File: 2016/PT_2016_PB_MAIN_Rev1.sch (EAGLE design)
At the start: 126 parts, among them Q1 Q_IRFS7437PbF, Q11 Q_IRFS7437PbF, Q12 2N7002, Q14 Q_IRFS7437PbF, Q16 Q_IRFS7437PbF, Q2 2N7002, Q20 Q_IRFS7437PbF, Q6 Q_IRFS7437PbF, Q7 Q_IRFS7437PbF, Q9 Q_IRFS7437PbF

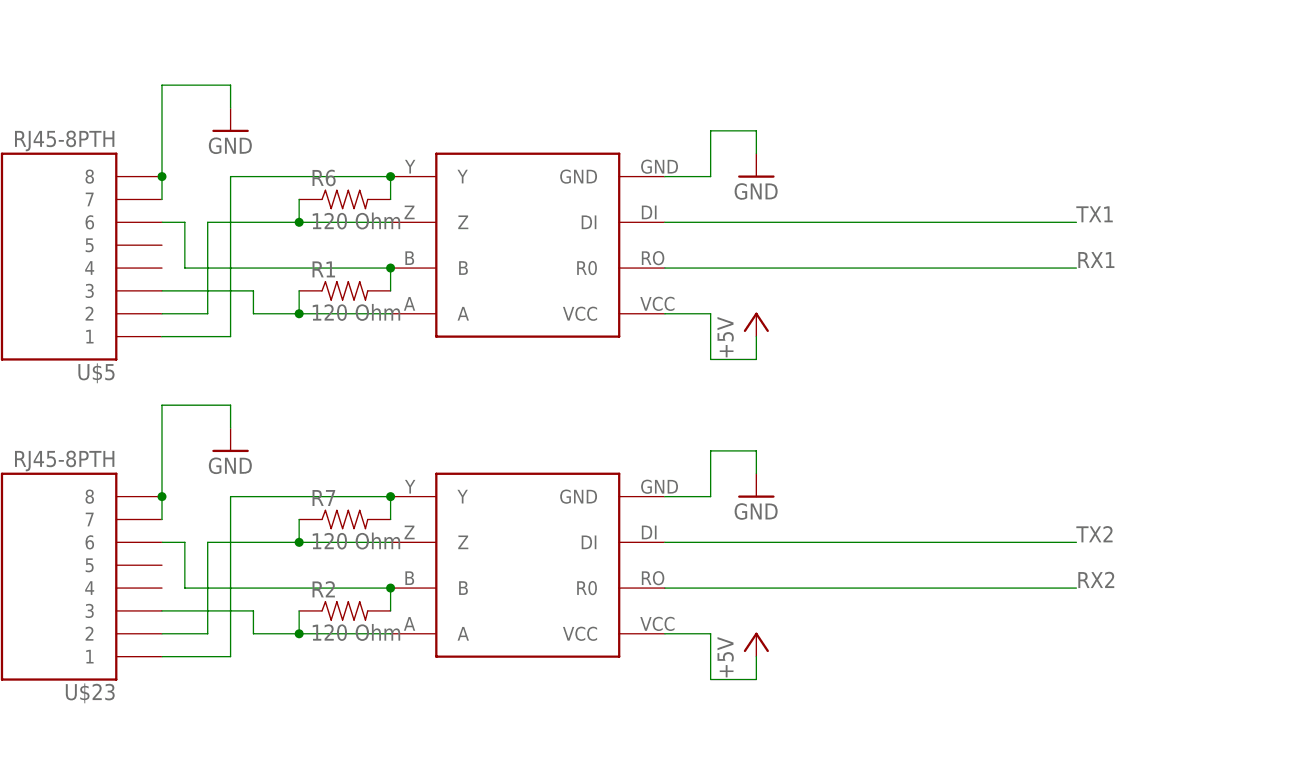
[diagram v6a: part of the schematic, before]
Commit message: changed connections for rj45
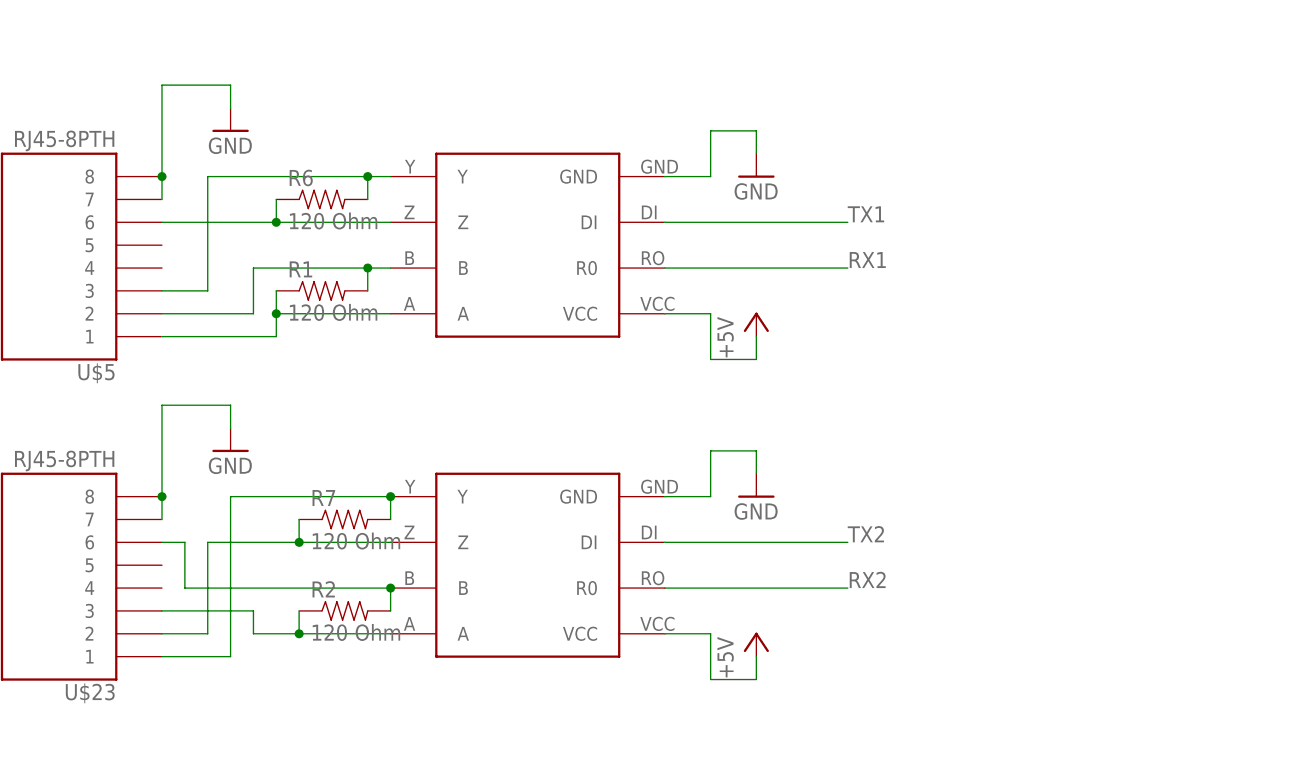
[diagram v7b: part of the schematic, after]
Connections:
- net N$11 renamed TRANS-_2
- net N$32 renamed TRANS+_2
- net N$5 renamed REC+_2
- net N$8 renamed REC-_2
- removed net N$18: R6.1, U$12.Z, U$5.2
- removed net N$19: R1.2, U$12.B, U$5.6
- removed net N$20: R1.1, U$12.A, U$5.3
- removed net N$3: R6.2, U$12.Y, U$5.1
- new net REC+: R1.1, U$12.A, U$5.1
- new net REC-: R1.2, U$12.B, U$5.2
- new net TRANS+: R6.2, U$12.Y, U$5.3
- new net TRANS-: R6.1, U$12.Z, U$5.6
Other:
- moved on the sheet: R1, R6
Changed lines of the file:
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@@
 <instance part="U$4" gate="G$1" x="-162.56" y="-147.32"/>
 <instance part="U$5" gate="G$1" x="-462.28" y="-53.34" rot="R180"/>
-<instance part="R1" gate="G$1" x="-429.26" y="-58.42"/>
-<instance part="R6" gate="G$1" x="-429.26" y="-48.26"/>
+<instance part="R1" gate="G$1" x="-431.8" y="-58.42"/>
+<instance part="R6" gate="G$1" x="-431.8" y="-48.26"/>
 <instance part="GND16" gate="1" x="-383.54" y="-45.72"/>
 <instance part="P+6" gate="1" x="-383.54" y="-60.96"/>
@@
 <net name="RX1" class="0">
 <segment>
-<wire x1="-347.98" y1="-55.88" x2="-393.7" y2="-55.88" width="0.1524" layer="91"/>
+<wire x1="-373.38" y1="-55.88" x2="-393.7" y2="-55.88" width="0.1524" layer="91"/>
 <pinref part="U$12" gate="G$1" pin="R0"/>
-<label x="-347.98" y="-55.88" size="1.778" layer="95"/>
+<label x="-373.38" y="-55.88" size="1.778" layer="95"/>
 </segment>
 <segment>
@@
 </segment>
 </net>
-<net name="N$3" class="0">
-<segment>
-<wire x1="-424.18" y1="-45.72" x2="-441.96" y2="-45.72" width="0.1524" layer="91"/>
-<wire x1="-441.96" y1="-45.72" x2="-441.96" y2="-63.5" width="0.1524" layer="91"/>
+<net name="REC+" class="0">
+<segment>
 <pinref part="U$5" gate="G$1" pin="1"/>
-<wire x1="-441.96" y1="-63.5" x2="-449.58" y2="-63.5" width="0.1524" layer="91"/>
+<wire x1="-424.18" y1="-60.96" x2="-436.88" y2="-60.96" width="0.1524" layer="91"/>
+<pinref part="R1" gate="G$1" pin="1"/>
+<wire x1="-436.88" y1="-58.42" x2="-436.88" y2="-60.96" width="0.1524" layer="91"/>
+<pinref part="U$12" gate="G$1" pin="A"/>
+<wire x1="-449.58" y1="-63.5" x2="-436.88" y2="-63.5" width="0.1524" layer="91"/>
+<wire x1="-436.88" y1="-63.5" x2="-436.88" y2="-60.96" width="0.1524" layer="91"/>
+<junction x="-436.88" y="-60.96"/>
+</segment>
+</net>
+<net name="REC-" class="0">
+<segment>
+<pinref part="U$5" gate="G$1" pin="2"/>
+<wire x1="-449.58" y1="-60.96" x2="-439.42" y2="-60.96" width="0.1524" layer="91"/>
+<wire x1="-439.42" y1="-60.96" x2="-439.42" y2="-55.88" width="0.1524" layer="91"/>
+<pinref part="R1" gate="G$1" pin="2"/>
+<wire x1="-426.72" y1="-58.42" x2="-426.72" y2="-55.88" width="0.1524" layer="91"/>
+<wire x1="-424.18" y1="-55.88" x2="-426.72" y2="-55.88" width="0.1524" layer="91"/>
+<pinref part="U$12" gate="G$1" pin="B"/>
+<wire x1="-439.42" y1="-55.88" x2="-426.72" y2="-55.88" width="0.1524" layer="91"/>
+<junction x="-426.72" y="-55.88"/>
+</segment>
+</net>
+<net name="TRANS+" class="0">
+<segment>
+<pinref part="U$5" gate="G$1" pin="3"/>
+<wire x1="-449.58" y1="-58.42" x2="-444.5" y2="-58.42" width="0.1524" layer="91"/>
+<wire x1="-444.5" y1="-58.42" x2="-444.5" y2="-45.72" width="0.1524" layer="91"/>
+<wire x1="-424.18" y1="-45.72" x2="-426.72" y2="-45.72" width="0.1524" layer="91"/>
+<pinref part="U$12" gate="G$1" pin="Y"/>
 <pinref part="R6" gate="G$1" pin="2"/>
-<wire x1="-424.18" y1="-45.72" x2="-424.18" y2="-48.26" width="0.1524" layer="91"/>
-<pinref part="U$12" gate="G$1" pin="Y"/>
-<junction x="-424.18" y="-45.72"/>
-</segment>
-</net>
-<net name="N$18" class="0">
-<segment>
-<wire x1="-424.18" y1="-50.8" x2="-434.34" y2="-50.8" width="0.1524" layer="91"/>
-<wire x1="-434.34" y1="-50.8" x2="-444.5" y2="-50.8" width="0.1524" layer="91"/>
-<wire x1="-444.5" y1="-50.8" x2="-444.5" y2="-60.96" width="0.1524" layer="91"/>
-<pinref part="U$5" gate="G$1" pin="2"/>
-<wire x1="-444.5" y1="-60.96" x2="-449.58" y2="-60.96" width="0.1524" layer="91"/>
-<pinref part="R6" gate="G$1" pin="1"/>
-<wire x1="-434.34" y1="-48.26" x2="-434.34" y2="-50.8" width="0.1524" layer="91"/>
-<junction x="-434.34" y="-50.8"/>
-<pinref part="U$12" gate="G$1" pin="Z"/>
-</segment>
-</net>
-<net name="N$19" class="0">
-<segment>
-<wire x1="-424.18" y1="-55.88" x2="-447.04" y2="-55.88" width="0.1524" layer="91"/>
-<wire x1="-447.04" y1="-55.88" x2="-447.04" y2="-50.8" width="0.1524" layer="91"/>
-<pinref part="U$5" gate="G$1" pin="6"/>
-<wire x1="-447.04" y1="-50.8" x2="-449.58" y2="-50.8" width="0.1524" layer="91"/>
-<pinref part="R1" gate="G$1" pin="2"/>
-<wire x1="-424.18" y1="-55.88" x2="-424.18" y2="-58.42" width="0.1524" layer="91"/>
-<pinref part="U$12" gate="G$1" pin="B"/>
-<junction x="-424.18" y="-55.88"/>
-</segment>
-</net>
-<net name="N$20" class="0">
-<segment>
-<wire x1="-424.18" y1="-60.96" x2="-434.34" y2="-60.96" width="0.1524" layer="91"/>
-<wire x1="-434.34" y1="-60.96" x2="-439.42" y2="-60.96" width="0.1524" layer="91"/>
-<wire x1="-439.42" y1="-60.96" x2="-439.42" y2="-58.42" width="0.1524" layer="91"/>
-<pinref part="U$5" gate="G$1" pin="3"/>
-<wire x1="-439.42" y1="-58.42" x2="-449.58" y2="-58.42" width="0.1524" layer="91"/>
-<pinref part="R1" gate="G$1" pin="1"/>
-<wire x1="-434.34" y1="-58.42" x2="-434.34" y2="-60.96" width="0.1524" layer="91"/>
-<junction x="-434.34" y="-60.96"/>
-<pinref part="U$12" gate="G$1" pin="A"/>
+<wire x1="-426.72" y1="-48.26" x2="-426.72" y2="-45.72" width="0.1524" layer="91"/>
+<wire x1="-444.5" y1="-45.72" x2="-426.72" y2="-45.72" width="0.1524" layer="91"/>
+<junction x="-426.72" y="-45.72"/>
 </segment>
 </net>
 <net name="TX1" class="0">
 <segment>
-<wire x1="-393.7" y1="-50.8" x2="-347.98" y2="-50.8" width="0.1524" layer="91"/>
+<wire x1="-393.7" y1="-50.8" x2="-373.38" y2="-50.8" width="0.1524" layer="91"/>
 <pinref part="U$12" gate="G$1" pin="DI"/>
-<label x="-347.98" y="-50.8" size="1.778" layer="95"/>
+<label x="-373.38" y="-50.8" size="1.778" layer="95"/>
 </segment>
 <segment>
@@
 <net name="RX2" class="0">
 <segment>
-<wire x1="-347.98" y1="-91.44" x2="-393.7" y2="-91.44" width="0.1524" layer="91"/>
+<wire x1="-373.38" y1="-91.44" x2="-393.7" y2="-91.44" width="0.1524" layer="91"/>
 <pinref part="U$24" gate="G$1" pin="R0"/>
-<label x="-347.98" y="-91.44" size="1.778" layer="95"/>
+<label x="-373.38" y="-91.44" size="1.778" layer="95"/>
 </segment>
 <segment>
@@
 </segment>
 </net>
-<net name="N$5" class="0">
+<net name="REC+_2" class="0">
 <segment>
 <wire x1="-424.18" y1="-81.28" x2="-441.96" y2="-81.28" width="0.1524" layer="91"/>
@@
 </segment>
 </net>
-<net name="N$8" class="0">
+<net name="REC-_2" class="0">
 <segment>
 <wire x1="-424.18" y1="-86.36" x2="-434.34" y2="-86.36" width="0.1524" layer="91"/>
@@
 </segment>
 </net>
-<net name="N$11" class="0">
+<net name="TRANS-_2" class="0">
 <segment>
 <wire x1="-424.18" y1="-91.44" x2="-447.04" y2="-91.44" width="0.1524" layer="91"/>
@@
 </segment>
 </net>
-<net name="N$32" class="0">
+<net name="TRANS+_2" class="0">
 <segment>
 <wire x1="-424.18" y1="-96.52" x2="-434.34" y2="-96.52" width="0.1524" layer="91"/>
@@
 <net name="TX2" class="0">
 <segment>
-<wire x1="-393.7" y1="-86.36" x2="-347.98" y2="-86.36" width="0.1524" layer="91"/>
+<wire x1="-393.7" y1="-86.36" x2="-373.38" y2="-86.36" width="0.1524" layer="91"/>
 <pinref part="U$24" gate="G$1" pin="DI"/>
-<label x="-347.98" y="-86.36" size="1.778" layer="95"/>
+<label x="-373.38" y="-86.36" size="1.778" layer="95"/>
 </segment>
 <segment>
@@
 </segment>
 </net>
+<net name="TRANS-" class="0">
+<segment>
+<pinref part="U$5" gate="G$1" pin="6"/>
+<wire x1="-424.18" y1="-50.8" x2="-436.88" y2="-50.8" width="0.1524" layer="91"/>
+<pinref part="R6" gate="G$1" pin="1"/>
+<wire x1="-436.88" y1="-48.26" x2="-436.88" y2="-50.8" width="0.1524" layer="91"/>
+<pinref part="U$12" gate="G$1" pin="Z"/>
+<wire x1="-449.58" y1="-50.8" x2="-436.88" y2="-50.8" width="0.1524" layer="91"/>
+<junction x="-436.88" y="-50.8"/>
+</segment>
+</net>

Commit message: swapped high current horiz o/p for vert, edited other rj45 connection
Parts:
- 12V-AUX, 5V-AUX, AUX_P, AUX_P2, MOTOR_1, MOTOR_2, MOTOR_3, MOTOR_4, MOTOR_5, MOTOR_6: value H_20020618-M02HORIZ -> H_20020618-M02VERT; device MRDT-2015-PowerBoard:H_20020618-M02HORIZ -> MRDT-2015-PowerBoard:H_20020618-M02VERT
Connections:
- removed net REC+_2: R7.2, U$23.1, U$24.Y
- removed net REC-_2: R7.1, U$23.2, U$24.Z
- removed net TRANS+_2: R2.1, U$23.3, U$24.A
- removed net TRANS-_2: R2.2, U$23.6, U$24.B
- new net REC+1: R2.1, U$23.1, U$24.A
- new net REC-1: R2.2, U$23.2, U$24.B
- new net TRANS+1: R7.2, U$23.3, U$24.Y
- new net TRANS-1: R7.1, U$23.6, U$24.Z
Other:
- moved on the sheet: R2, R7
